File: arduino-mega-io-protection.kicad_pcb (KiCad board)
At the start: 4 copper layers, 150.1 x 72 mm, 158 parts, among them J101 CONN_01X02, J102 CONN_01X02, J103 CONN_01X02, J104 CONN_01X02, J105 CONN_01X02, J106 CONN_01X02, J107 CONN_01X02, J108 CONN_01X36, J109 CONN_01X10, J110 CONN_02X18, J111 CONN_01X08, J112 CONN_01X08, J113 CONN_01X08, J114 CONN_01X08, J115 CONN_01X08, J116 CONN_01X02, J117 CONN_01X02, J118 CONN_01X02, U201 MOCD217M, U202 MOCD217M, U203 MOCD217M, U204 MOCD217M, U205 MOCD217M, U206 MOCD217M, U207 MOCD217M, U208 MOCD217M, U209 MOCD217M, U210 MOCD217M, U211 MOCD217M, U212 MOCD217M, U213 MOCD217M, U214 MOCD217M, U215 MOCD217M, U216 MOCD217M, U217 MOCD217M, U218 MOCD217M, U219 MOCD217M, U220 MOCD217M, U221 MOCD217M, U222 MOCD217M, U223 MOCD217M, U224 MOCD217M, U225 MOCD217M

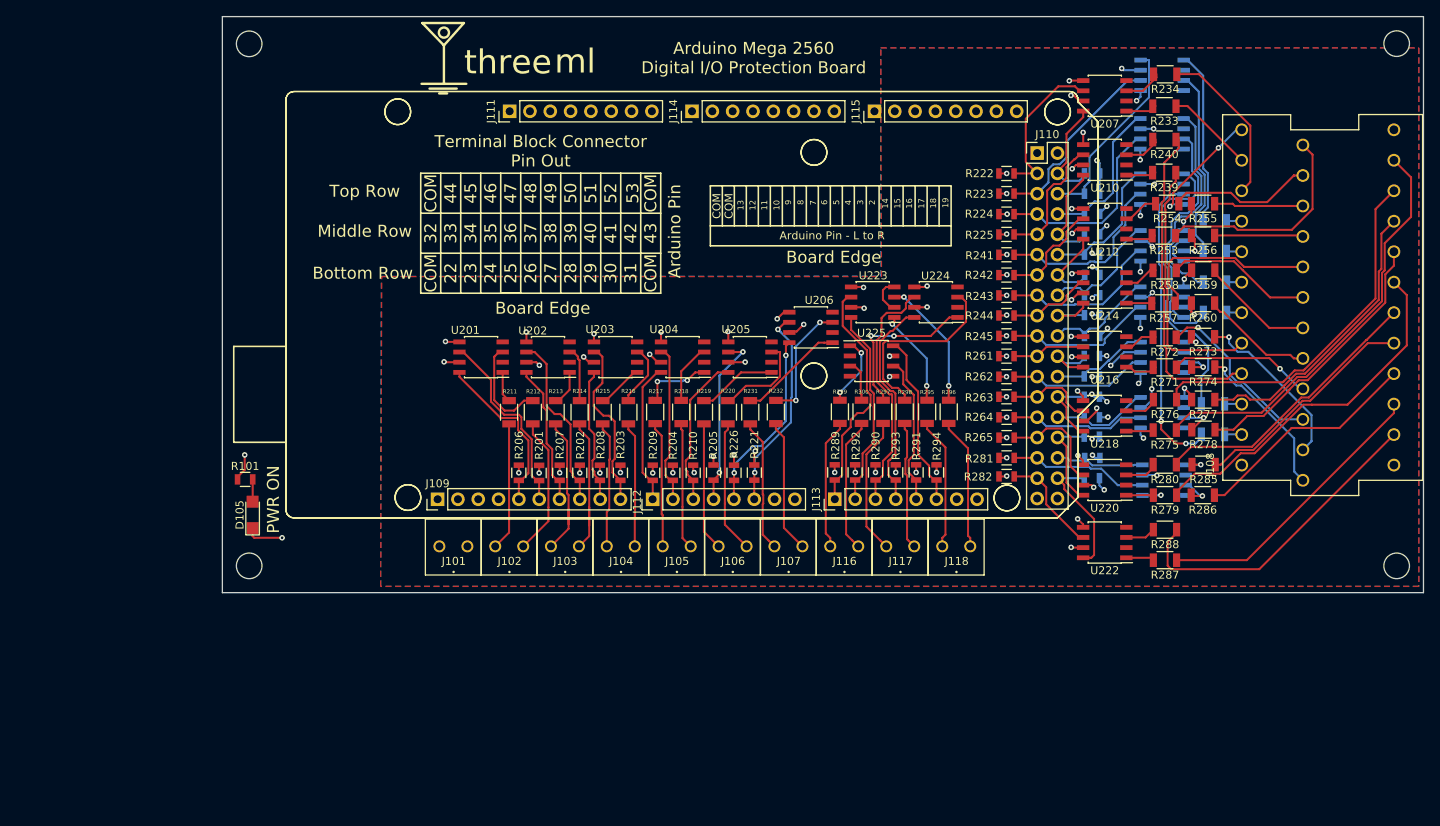
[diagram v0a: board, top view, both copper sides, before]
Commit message: more work on ethernet layout
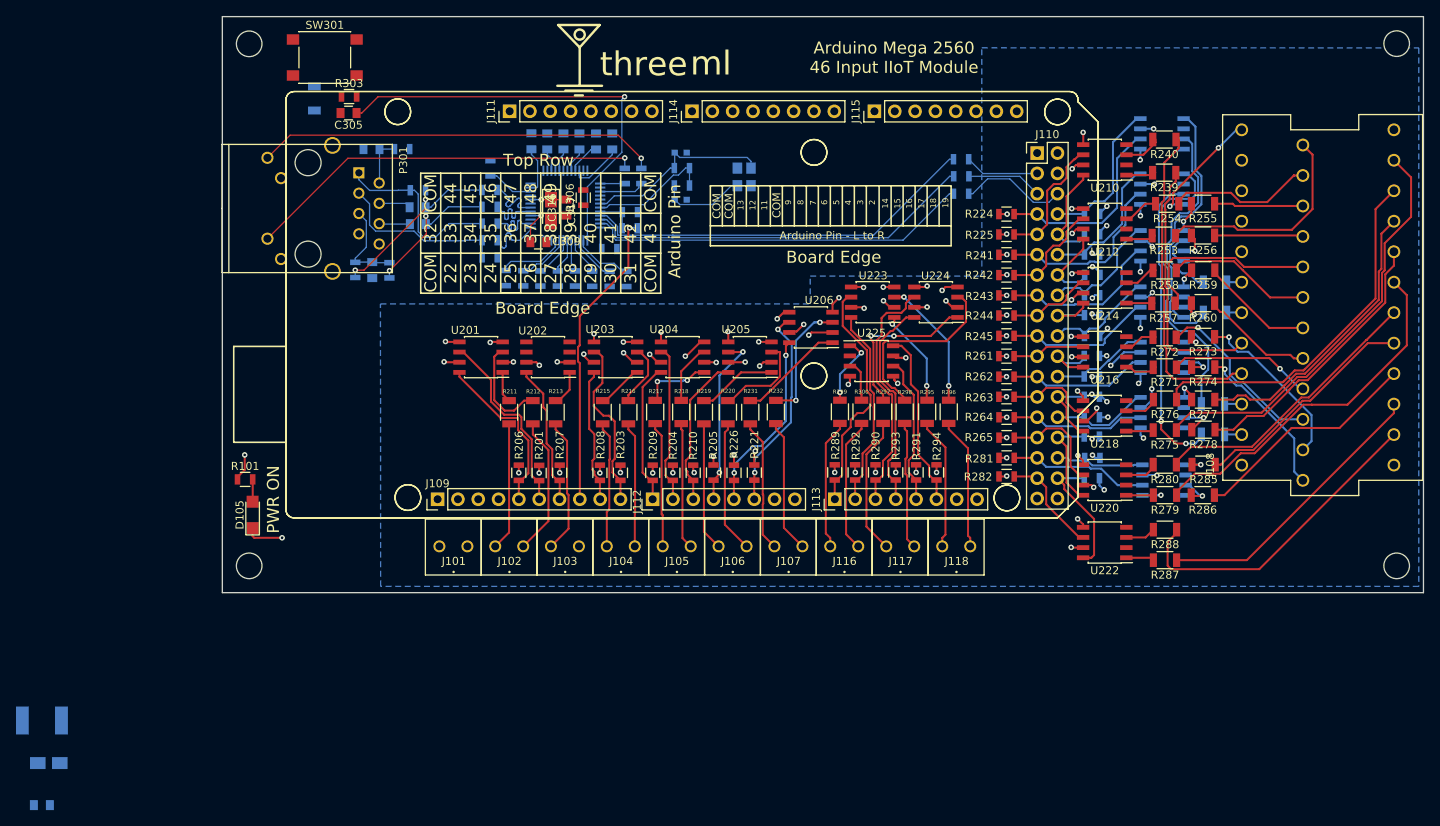
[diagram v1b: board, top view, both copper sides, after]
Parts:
- removed R202, R222, R223, R227, R228: 10K, Resistors_SMD:R_0805
- removed R214, R233, R234, R235, R236: 4.8k, Resistors_SMD:R_1206
- removed U207, U208: MOCD217M, Housings_SOIC:SOIC-8_3.9x4.9mm_Pitch1.27mm
- added C301: 18pF, Capacitors_SMD:C_0603, B.Cu at (131.7, 96.7)
- added C302: 18pF, Capacitors_SMD:C_0603, B.Cu at (131.7, 90.8)
- added C303: 0.1uF, Capacitors_SMD:C_0805, B.Cu at (51.9, 172.4)
- added C304: 10uF/16V, Capacitors_Tantalum_SMD:CP_Tantalum_Case-A_EIA-3216-18_Reflow, B.Cu at (52.8, 167.1)
- added C305: 0.1uF, Capacitors_SMD:C_0805, F.Cu at (90.2, 85.9)
- added C306: 10nF, Capacitors_SMD:C_0805, B.Cu at (123.2, 89.4)
- added C307: 4.7uF, Capacitors_SMD:C_0805, B.Cu at (119.1, 89.4)
- added C308: 0.1uF, Capacitors_SMD:C_0805, B.Cu at (115.1, 89.4)
- added C309: 0.1uF, Capacitors_SMD:C_0805, F.Cu at (114.0, 102.0)
- added C310: 0.1uF, Capacitors_SMD:C_0805, B.Cu at (117.1, 89.4)
- added C311: 0.1uF, Capacitors_SMD:C_0805, B.Cu at (121.2, 89.4)
- added C312: 10nF, Capacitors_SMD:C_0805, B.Cu at (93.2, 105.5)
- added C313: 0.1uF, Capacitors_SMD:C_0805, B.Cu at (113.1, 89.4)
- added C314: 6.8nF, Capacitors_SMD:C_0805, B.Cu at (98.9, 97.6)
- added C315: 6.8nF, Capacitors_SMD:C_0805, B.Cu at (98.9, 99.7)
- added C316: 0.1uF, Capacitors_SMD:C_0805, F.Cu at (117.4, 97.7)
- added C317: 10uF/16V, Capacitors_Tantalum_SMD:CP_Tantalum_Case-A_EIA-3216-18_Reflow, F.Cu at (115.5, 98.1)
- added C318: 22nF, Capacitors_SMD:C_0805, B.Cu at (93.1, 90.4)
- added C319: 1nF/2kV, Capacitors_SMD:C_1206, B.Cu at (86.0, 84.0)
- added L301: L, Resistors_SMD:R_1812, B.Cu at (51.9, 161.8)
- added P301: J1B1211CCD, 3ML_W5500:J1B1211CCD, F.Cu at (85.2, 92.1)
- added R102: 0, Resistors_SMD:R_0805, B.Cu at (166.8, 95.9)
- added R103: 0, Resistors_SMD:R_0805, B.Cu at (166.8, 93.8)
- added R104: 0, Resistors_SMD:R_0805, B.Cu at (166.8, 91.6)
- added R105: 0, Resistors_SMD:R_0805, B.Cu at (125.4, 100.3)
- added R301: 0, Resistors_SMD:R_0805, B.Cu at (131.9, 94.9)
- added R302: 1M, Resistors_SMD:R_0805, B.Cu at (131.9, 92.7)
- added R303: 10K, Resistors_SMD:R_0805, F.Cu at (90.3, 83.8)
- added R304: 10K, Resistors_SMD:R_0805, B.Cu at (122.8, 102.9)
- added R305: 10K, Resistors_SMD:R_0805, B.Cu at (125.4, 98.2)
- added R306: 10K, Resistors_SMD:R_0805, F.Cu at (119.6, 96.4)
- added R307: 10K, Resistors_SMD:R_0805, B.Cu at (124.9, 106.6)
- added R308: 10K, Resistors_SMD:R_0805, B.Cu at (122.9, 106.6)
- added R309: 10K, Resistors_SMD:R_0805, B.Cu at (120.7, 106.6)
- added R310: 10K, Resistors_SMD:R_0805, B.Cu at (118.5, 106.6)
- added R311: 10K, Resistors_SMD:R_0805, B.Cu at (116.4, 106.6)
- added R312: 10K, Resistors_SMD:R_0805, B.Cu at (114.2, 106.6)
- added R313: 10K, Resistors_SMD:R_0805, B.Cu at (112.1, 106.5)
- added R314: 10K, Resistors_SMD:R_0805, B.Cu at (109.9, 106.5)
- added R315: 12.4K, Resistors_SMD:R_0805, B.Cu at (108.0, 92.8)
- added R316: 33, Resistors_SMD:R_0805, B.Cu at (107.9, 99.7)
- added R317: 33, Resistors_SMD:R_0805, B.Cu at (107.9, 101.8)
- added R318: 33, Resistors_SMD:R_0805, B.Cu at (107.8, 95.5)
- added R319: 33, Resistors_SMD:R_0805, B.Cu at (107.8, 97.6)
- added R320: 49.9, Resistors_SMD:R_0805, B.Cu at (91.1, 105.5)
- added R321: 49.9, Resistors_SMD:R_0805, B.Cu at (95.3, 105.5)
- added R322: 49.9, Resistors_SMD:R_0805, B.Cu at (107.9, 103.9)
- added R323: 49.9, Resistors_SMD:R_0805, B.Cu at (98.9, 95.5)
- added R324: 10, Resistors_SMD:R_0805, B.Cu at (96.9, 90.4)
- added R325: 330, Resistors_SMD:R_0805, B.Cu at (124.8, 93.7)
- added R326: 330, Resistors_SMD:R_0805, B.Cu at (126.8, 93.7)
- added SW301: SW_Push, Buttons_Switches_SMD:SW_SPST_PTS645, F.Cu at (87.3, 78.9)
- added U301: W5500, Housings_QFP:LQFP-48_7x7mm_Pitch0.5mm, B.Cu at (117.3, 97.4)
- added Y301: 25Mhz, 3ML_SMD_Generic:3ML_4-SMD, B.Cu at (139.7, 93.9)
- moved ACC106 17.0 mm to (119.1, 82.5)
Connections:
- J103 pad 2: /F_PWM10 -> GND
- J108 pad 32: /F_DIN50 -> (no net)
- J108 pad 33: /F_DIN51 -> (no net)
- J108 pad 34: /F_DIN52 -> (no net)
- J108 pad 35: /F_DIN53 -> (no net)
- J110 pad 4: /DIN53 -> (no net)
- U202 pad 3: Net-(R214-Pad2) -> (no net)
- U202 pad 4: GND -> (no net)
- U202 pad 5: GNDD -> (no net)
- U202 pad 6: /PWM10 -> (no net)
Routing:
- net Net-(C305-Pad1): track 0.00 -> 54.2 mm, vias 0 -> 1
- net Net-(P301-Pad9): track 0.00 -> 50.4 mm, vias 0 -> 1
- net Net-(P301-Pad11): track 0.00 -> 50.2 mm, vias 0 -> 1
- net /W5500/ARD_SCLK: track 0.00 -> 49.9 mm
- net /W5500/ARD_MISO: track 0.00 -> 49.1 mm
- net /W5500/ARD_MOSI: track 0.00 -> 48.0 mm
- net GND: track 28.9 -> 54.4 mm, vias 2 -> 18
- net Net-(C308-Pad1): track 0.00 -> 25.5 mm, vias 0 -> 2
- net /W5500/XI/CLKN: track 0.00 -> 23.9 mm
- net Net-(R236-Pad2): track 23.6 -> 0.00 mm
- net Net-(C314-Pad2): track 0.00 -> 23.5 mm, vias 0 -> 2
- net Net-(P301-Pad1): track 0.00 -> 23.0 mm
- net Net-(R235-Pad2): track 21.9 -> 0.00 mm
- net Net-(P301-Pad3): track 0.00 -> 21.6 mm
- net /F_DIN52: track 20.1 -> 0.00 mm
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- removed copper zone on F.Cu, net GND
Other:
- board text added: "Arduino Mega 2560 46 Input IIoT Module"
- board text removed: "10"
- board text removed: "50"
- board text removed: "51"
- board text removed: "52"
- board text removed: "53"
- board text removed: "Arduino Mega 2560 Digital I/O Protection Board"
- board text removed: "Bottom Row"
- board text removed: "Middle Row"
- board text removed: "Terminal Block Connector Pin Out"

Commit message: more tweaks
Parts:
- C303, C304, L301: moved to F.Cu
- C309, C316, C317, R306: moved to B.Cu
- moved L301 101.4 mm to (112.3, 80.3)
- moved C303 101.2 mm to (120.0, 97.5)
- moved C304 98.8 mm to (120.3, 95.1)
- moved C317 14.4 mm to (105.4, 108.3)
- moved R306 10.5 mm to (128.9, 91.7)
- moved C316 10.5 mm to (111.1, 89.4), turned to 90 degrees
- moved C309 8.56 mm to (107.7, 107.9), turned to 270 degrees
- moved R103 1.00 mm to (165.8, 93.8)
- moved R102 0.99 mm to (165.8, 95.9)
- moved R104 0.98 mm to (165.8, 91.6)
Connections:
- C301 pad 2: GND -> GNDD
- C302 pad 2: GND -> GNDD
- C303 pad 2: GND -> GNDD
- C304 pad 2: GND -> GNDD
- C305 pad 2: GND -> GNDD
- C306 pad 2: GND -> GNDD
- C307 pad 2: GND -> GNDD
- C308 pad 2: GND -> GNDD
- C309 pad 2: GND -> GNDD
- C310 pad 2: GND -> GNDD
- C311 pad 2: GND -> GNDD
- C312 pad 2: GND -> GNDD
- C313 pad 2: GND -> GNDD
- C316 pad 2: GND -> GNDD
- C317 pad 2: GND -> GNDD
- C318 pad 2: GND -> GNDD
- C319 pad 2: GND -> GNDD
- J111 pad 4: (no net) -> +3V3
- J111 pad 5: +5V -> (no net)
- R306 pad 2: GND -> GNDD
- R307 pad 1: GND -> GNDD
- R308 pad 1: GND -> GNDD
- R309 pad 1: GND -> GNDD
- R310 pad 1: GND -> GNDD
- R311 pad 1: GND -> GNDD
- R315 pad 2: GND -> GNDD
- SW301 pad 1: GND -> GNDD
- U301 pad 14: GND -> GNDD
- U301 pad 16: GND -> GNDD
- U301 pad 19: GND -> GNDD
- U301 pad 29: GND -> GNDD
- U301 pad 3: GND -> GNDD
- U301 pad 48: GND -> GNDD
- U301 pad 9: GND -> GNDD
- Y301 pad 2: GND -> GNDD
- Y301 pad 4: GND -> GNDD
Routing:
- net GNDD: track 81.5 -> 144.0 mm, vias 46 -> 78
- net +3V3: track 0.00 -> 34.2 mm, vias 0 -> 11
- net Net-(C308-Pad1): track 25.5 -> 44.4 mm, vias 2 -> 1
- net Net-(C305-Pad1): track 54.2 -> 67.3 mm
- net Net-(R306-Pad1): track 0.00 -> 11.6 mm, vias 0 -> 2
- net GND: track 54.4 -> 63.5 mm, vias 18 -> 23
- net Earth: track 0.00 -> 5.30 mm
- net Net-(C315-Pad2): track 18.8 -> 20.0 mm
- net /DIN50: track 9.45 -> 10.5 mm
- net /DIN51: track 13.5 -> 14.5 mm
- net /DIN52: track 9.32 -> 10.3 mm
- net Net-(C314-Pad2): track 23.5 -> 24.5 mm
- net /W5500/ARD_SCLK: track 49.9 -> 49.1 mm
- net /DIN44: track 22.9 -> 23.4 mm
- net /W5500/ARD_MISO: track 49.1 -> 48.5 mm
- added copper zone on PWR, net +3V3
- added copper zone on F.Cu, net GND
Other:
- board text added: "W5500 RST"

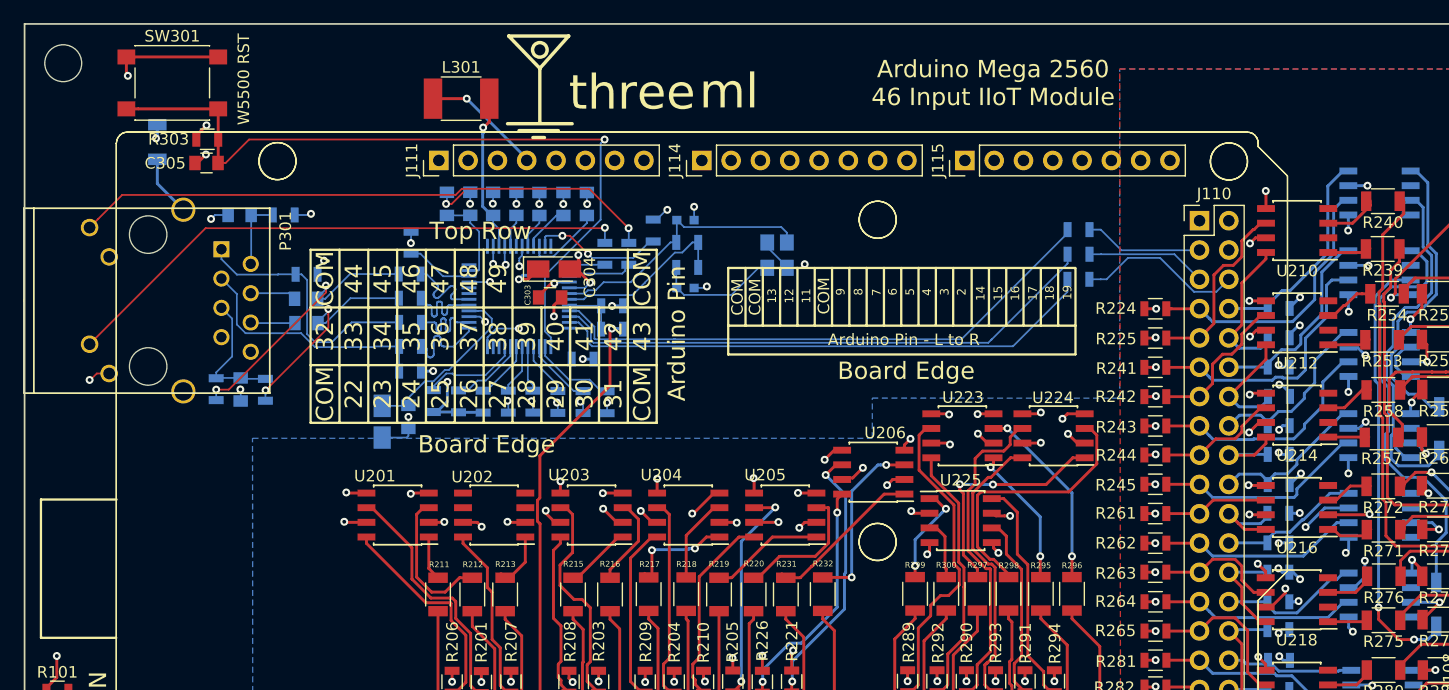
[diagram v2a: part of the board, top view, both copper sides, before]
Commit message: almost final design - just need to add protection diodes
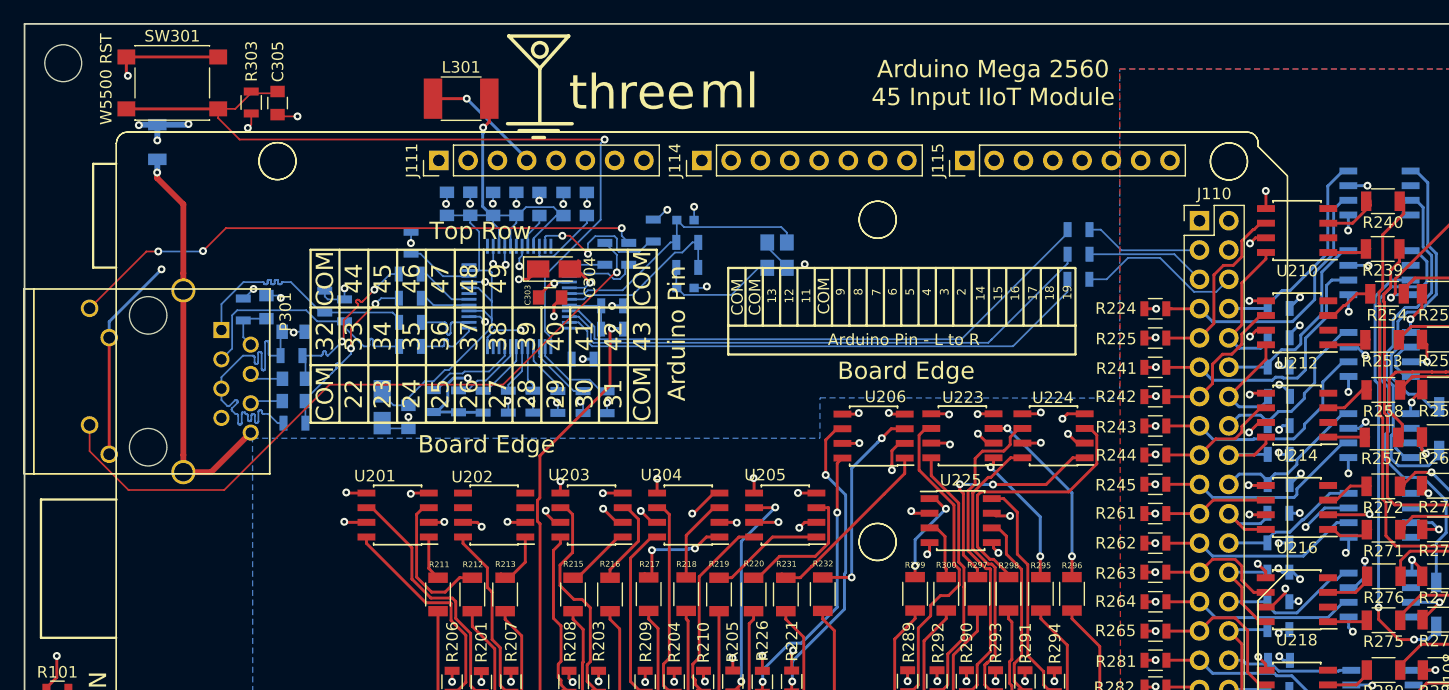
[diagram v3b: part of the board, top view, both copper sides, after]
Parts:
- moved R324 8.91 mm to (93.4, 98.6), turned to 270 degrees
- moved C318 8.32 mm to (95.4, 98.4), turned to 90 degrees
- moved C305 8.06 mm to (96.4, 80.7), turned to 270 degrees
- moved R322 7.75 mm to (102.2, 98.6), turned to 270 degrees
- moved R320 7.15 mm to (97.6, 102.6), turned to 180 degrees
- moved C314 7.01 mm to (97.8, 104.6)
- moved P301 7.00 mm to (85.2, 99.1)
- moved C315 6.84 mm to (97.8, 106.5)
- moved C312 6.80 mm to (97.8, 100.5), turned to 0 degrees
- moved R303 4.97 mm to (94.1, 80.6), turned to 90 degrees
- moved R321 3.83 mm to (97.8, 108.4), turned to 180 degrees
- moved U206 3.13 mm to (148.0, 109.5)
- moved R323 2.84 mm to (100.5, 97.9), turned to 270 degrees
- moved C317 1.26 mm to (105.4, 107.0)
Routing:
- net Earth: track 5.30 -> 35.4 mm, vias 0 -> 1
- net Net-(C308-Pad1): track 44.4 -> 62.4 mm
- net Net-(C312-Pad1): track 11.4 -> 29.3 mm
- net +3V3: track 34.2 -> 51.4 mm, vias 11 -> 10
- net Net-(P301-Pad11): track 50.2 -> 60.2 mm
- net Net-(C314-Pad2): track 24.5 -> 16.5 mm
- net Net-(C315-Pad2): track 20.0 -> 15.9 mm
- net Net-(R319-Pad2): track 8.00 -> 4.42 mm
- net /PWM3: track 23.3 -> 26.5 mm
- net /PWM2: track 26.0 -> 29.1 mm
- net Net-(R318-Pad2): track 8.00 -> 5.10 mm
- net Net-(R232-Pad2): track 15.5 -> 18.2 mm
- net Net-(R231-Pad2): track 13.8 -> 15.9 mm
- net Net-(R316-Pad2): track 8.02 -> 6.00 mm
- net Net-(R306-Pad1): track 11.6 -> 13.5 mm
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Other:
- net class Default: clearance 0.1524 -> 0.152; trace_width 0.254 -> 0.152
- rule trace_clearance: 0.1524 -> 0.152
- rule trace_min: 0.1524 -> 0.152
- board text added: "Arduino Mega 2560 45 Input IIoT Module"
- board text removed: "Arduino Mega 2560 46 Input IIoT Module"

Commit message: final design sent to fab
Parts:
- moved R302 3.92 mm to (131.9, 96.7)
- moved Y301 2.43 mm to (137.9, 95.6), turned to 270 degrees
- moved C302 2.42 mm to (132.0, 93.2), turned to 180 degrees
- moved C301 1.38 mm to (132.0, 98.1), turned to 180 degrees
- moved R324 1.09 mm to (93.4, 97.5)
- moved C318 1.09 mm to (95.4, 97.3)
- moved R301 0.29 mm to (131.9, 94.6), turned to 0 degrees
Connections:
- C301 pad 1: Net-(C301-Pad1) -> /W5500/X0
- C302 pad 1: /W5500/XI/CLKN -> Net-(C302-Pad1)
- R301 pad 1: /W5500/X0 -> /W5500/XI/CLKN
- R301 pad 2: Net-(C301-Pad1) -> Net-(C302-Pad1)
- Y301 pad 1: Net-(C301-Pad1) -> Net-(C302-Pad1)
- Y301 pad 3: /W5500/XI/CLKN -> /W5500/X0
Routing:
- net Net-(C312-Pad1): track 29.3 -> 16.4 mm
- net /W5500/XI/CLKN: track 23.9 -> 11.5 mm
- net Net-(C301-Pad1): track 10.9 -> 0.00 mm
- net Net-(C302-Pad1): track 0.00 -> 8.63 mm
- net GNDD: track 144.5 -> 142.3 mm, vias 79 -> 80
- net /W5500/X0: track 15.7 -> 17.7 mm
- net Net-(P301-Pad3): track 21.5 -> 20.1 mm
- net Net-(C318-Pad1): track 4.47 -> 5.36 mm
- net Net-(P301-Pad1): track 21.5 -> 20.6 mm
